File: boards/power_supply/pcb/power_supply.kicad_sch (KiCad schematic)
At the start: 0 parts

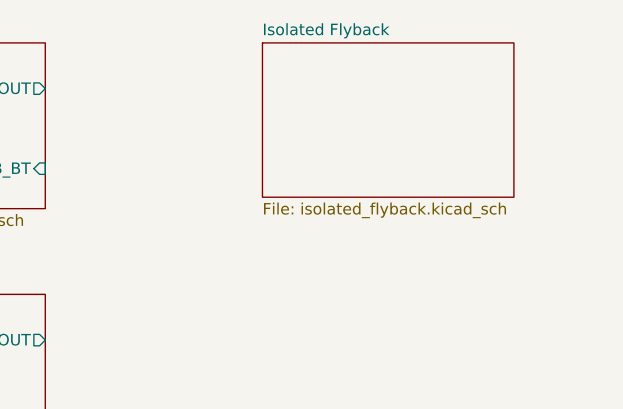
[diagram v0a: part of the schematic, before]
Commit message: psu schematic capture
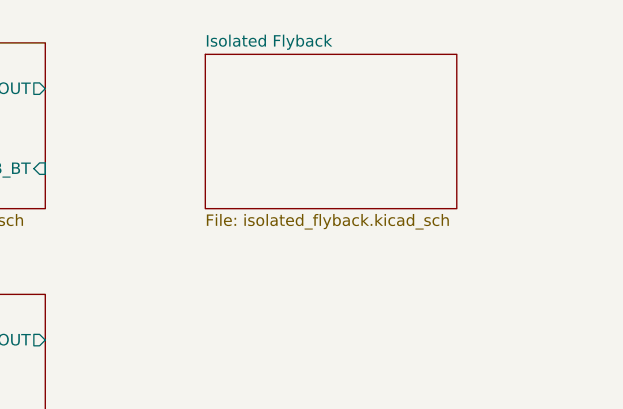
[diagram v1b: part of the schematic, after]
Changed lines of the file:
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@@
 	)
 	(sheet
-		(at 176.53 60.96)
+		(at 170.18 62.23)
 		(size 27.94 17.145)
 		(fields_autoplaced yes)
@@
 		)
 		(property "Sheetname" "Isolated Flyback"
-			(at 176.53 60.2484 0)
+			(at 170.18 61.5184 0)
 			(effects
 				(font
@@
 		)
 		(property "Sheetfile" "isolated_flyback.kicad_sch"
-			(at 176.53 78.6896 0)
+			(at 170.18 79.9596 0)
 			(effects
 				(font

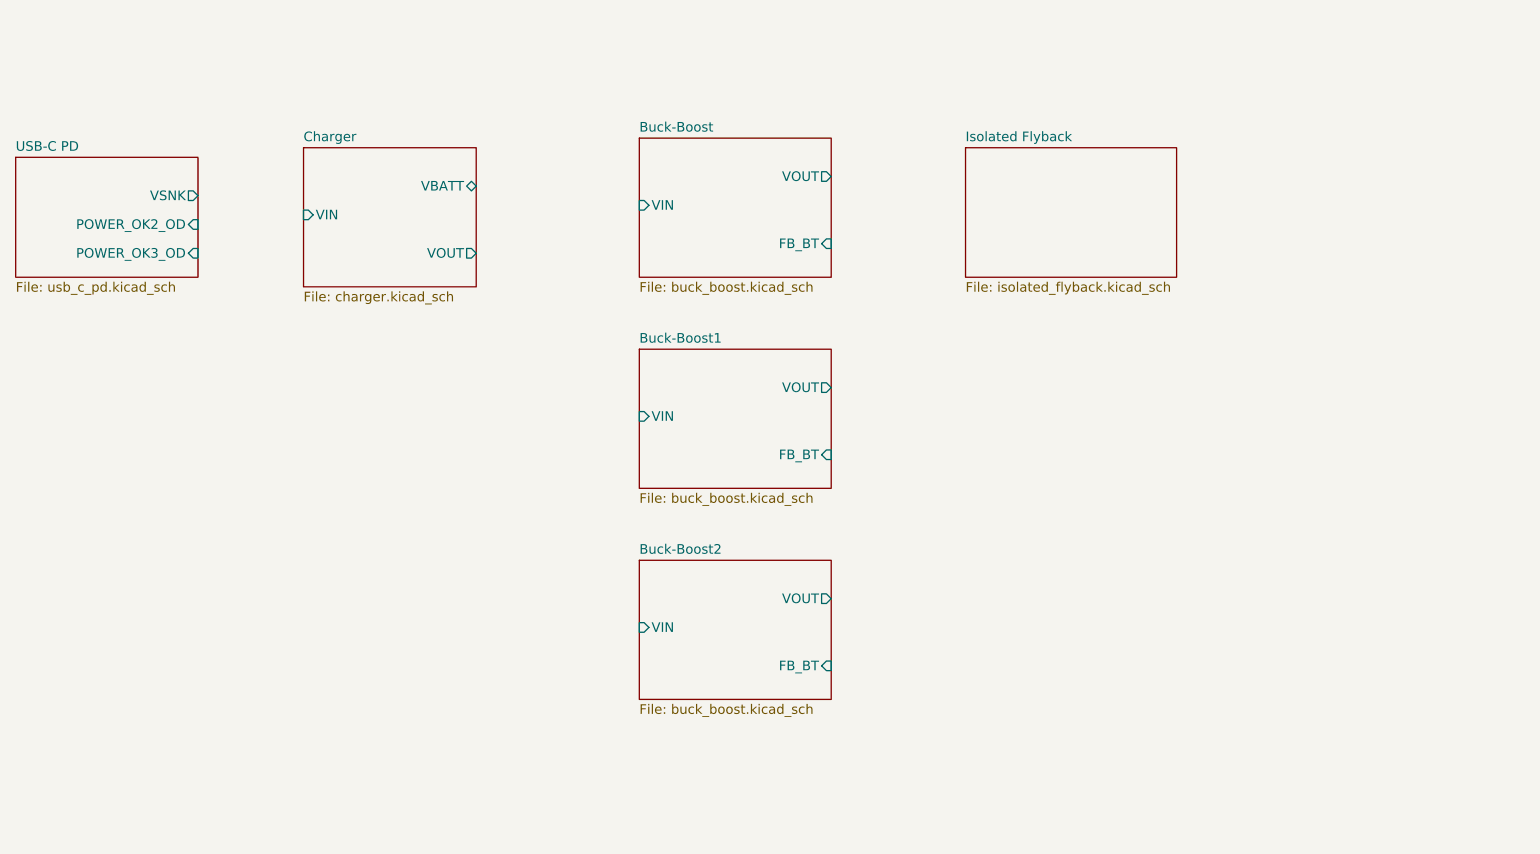
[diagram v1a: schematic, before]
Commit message: psu schematic capture
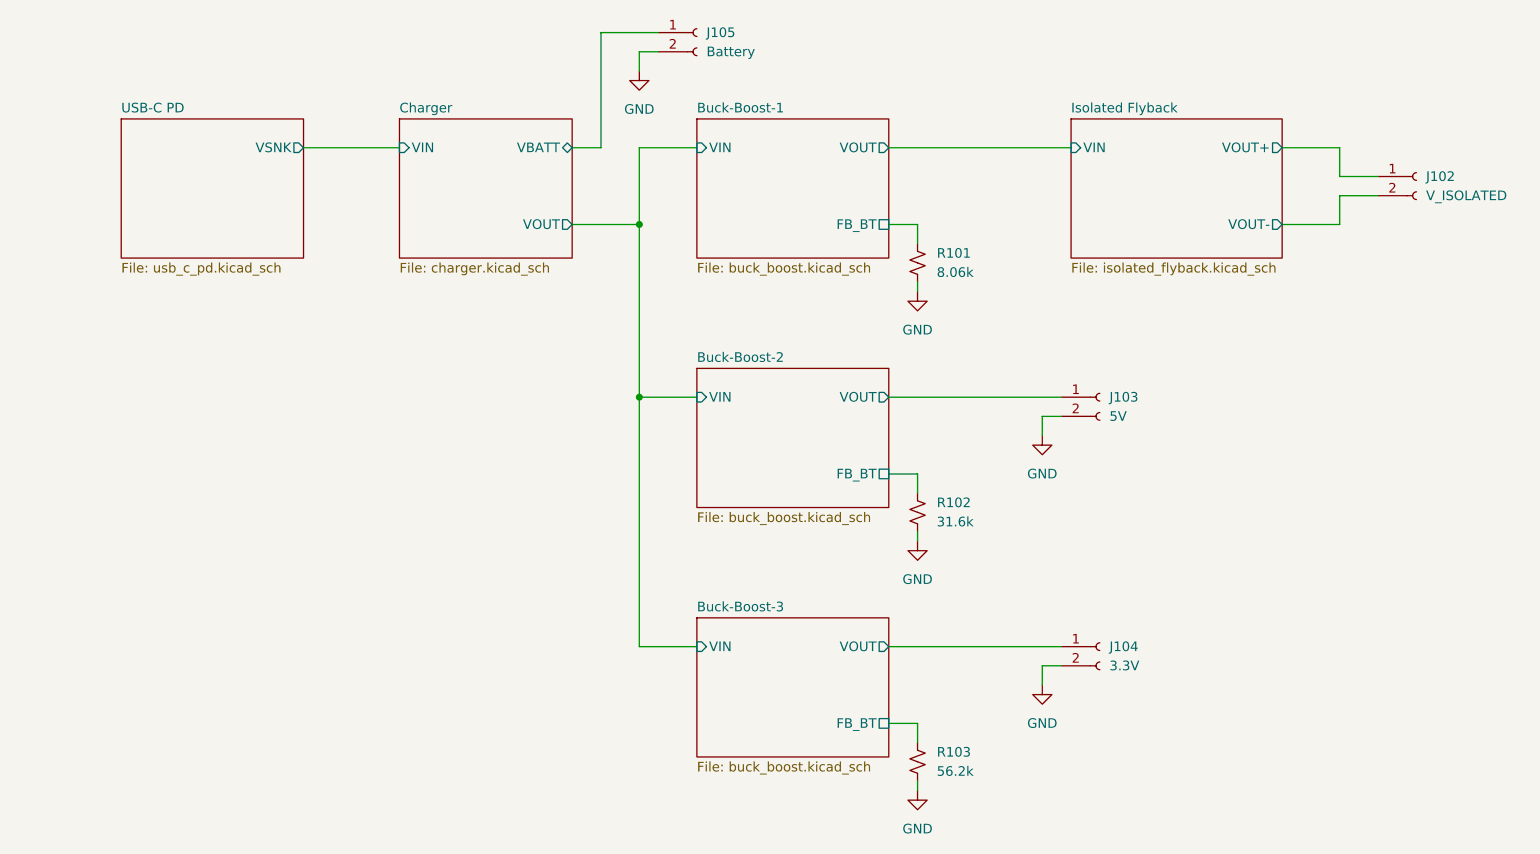
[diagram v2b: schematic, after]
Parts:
- added J102: V_ISOLATED, symbol Connector:Conn_01x02_Socket
- added J103: 5V, symbol Connector:Conn_01x02_Socket
- added J104: 3.3V, symbol Connector:Conn_01x02_Socket
- added J105: Battery, symbol Connector:Conn_01x02_Socket
- added R101: 8.06k, symbol Device:R_Small_US
- added R102: 31.6k, symbol Device:R_Small_US
- added R103: 56.2k, symbol Device:R_Small_US
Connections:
- net Buck-Boost-1/FB_BT: now also R101.2
- net Buck-Boost-2/FB_BT: now also R102.2
- net Buck-Boost-2/VOUT: now also J103.1 (Pin_1)
- net Buck-Boost-3/FB_BT: now also R103.2
- net Buck-Boost-3/VOUT: now also J104.1 (Pin_1)
- net Charger/VBATT: now also J105.1 (Pin_1)
- new net GND: J103.2 (Pin_2), J104.2 (Pin_2), J105.2 (Pin_2), R101.1, R102.1, R103.1
- new net Isolated Flyback/VOUT+: J102.1 (Pin_1)
- new net Isolated Flyback/VOUT-: J102.2 (Pin_2)
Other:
- sheet Buck-Boost renamed Buck-Boost-1
- sheet Buck-Boost1 renamed Buck-Boost-2
- sheet Buck-Boost2 renamed Buck-Boost-3
- sheet Isolated Flyback ports: added VIN, VOUT+, VOUT-; removed none
- sheet USB-C PD ports: added none; removed POWER_OK2_OD, POWER_OK3_OD

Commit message: psu component selection
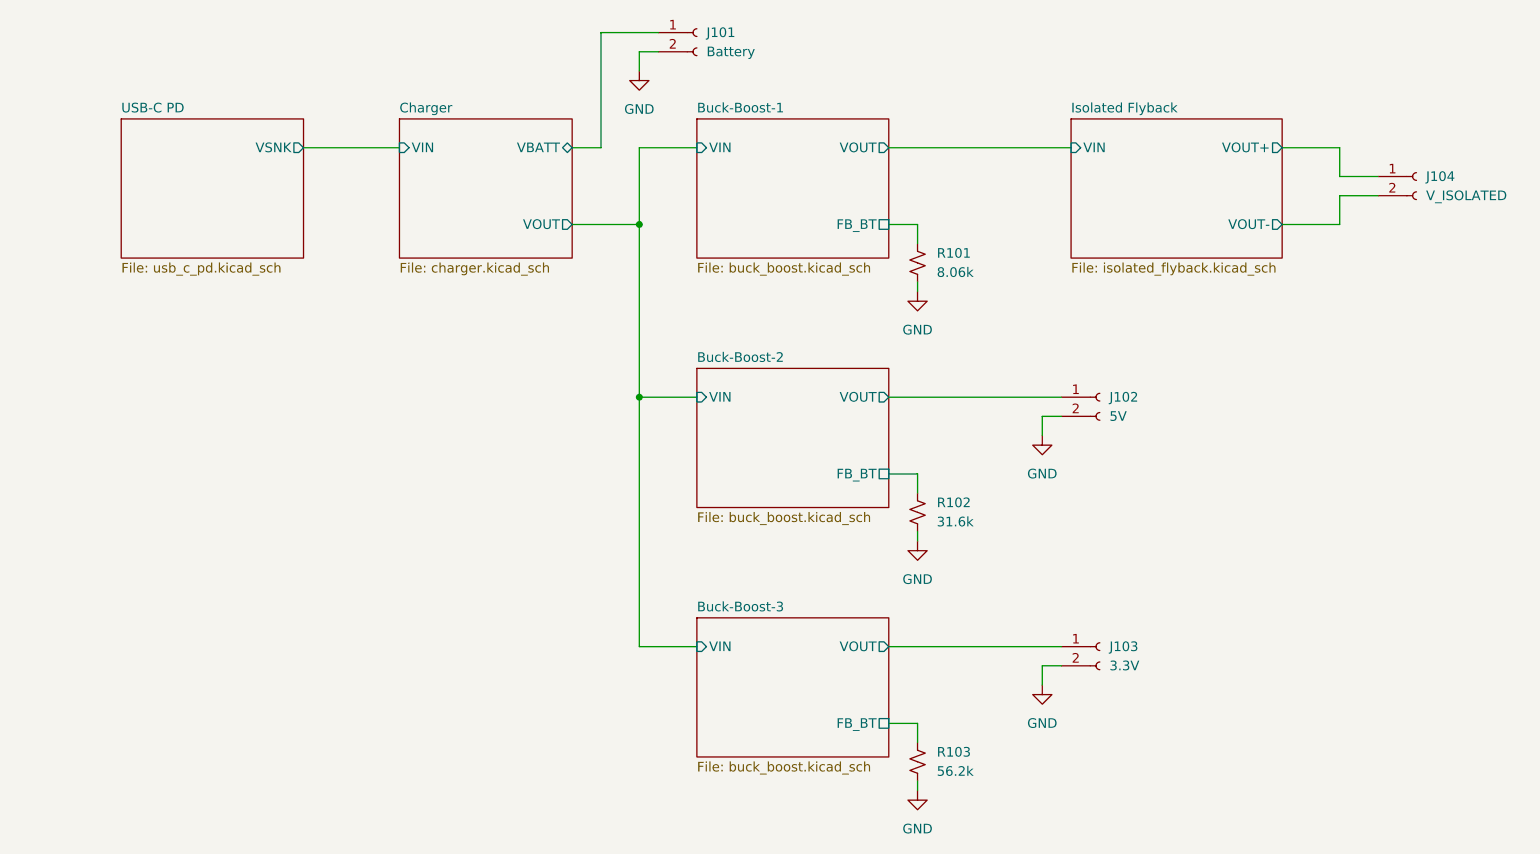
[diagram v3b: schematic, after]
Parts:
- renumbered J105 to J101, J103 to J102, J104 to J103, J102 to J104
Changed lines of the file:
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@@
 		(dnp no)
 		(fields_autoplaced yes)
-		(property "Reference" "J103"
+		(property "Reference" "J102"
 			(at 189.23 95.2499 0)
 			(effects
@@
 			(project "power_supply"
 				(path "/6a7d9dc9-f78f-470f-911b-b95256023173"
-					(reference "J103")
+					(reference "J102")
 					(unit 1)
 				)
@@
 		(dnp no)
 		(fields_autoplaced yes)
-		(property "Reference" "J104"
+		(property "Reference" "J103"
 			(at 189.23 128.2699 0)
 			(effects
@@
 			(project "power_supply"
 				(path "/6a7d9dc9-f78f-470f-911b-b95256023173"
-					(reference "J104")
+					(reference "J103")
 					(unit 1)
 				)
@@
 		(dnp no)
 		(fields_autoplaced yes)
-		(property "Reference" "#PWR0106"
+		(property "Reference" "#PWR0105"
 			(at 180.34 106.68 0)
 			(effects
@@
 			(project "power_supply"
 				(path "/6a7d9dc9-f78f-470f-911b-b95256023173"
-					(reference "#PWR0106")
+					(reference "#PWR0105")
 					(unit 1)
 				)
@@
 		(dnp no)
 		(fields_autoplaced yes)
-		(property "Reference" "J105"
+		(property "Reference" "J101"
 			(at 135.89 46.9899 0)
 			(effects
@@
 			(project "power_supply"
 				(path "/6a7d9dc9-f78f-470f-911b-b95256023173"
-					(reference "J105")
+					(reference "J101")
 					(unit 1)
 				)
@@
 		(dnp no)
 		(fields_autoplaced yes)
-		(property "Reference" "#PWR0105"
+		(property "Reference" "#PWR0106"
 			(at 180.34 139.7 0)
 			(effects
@@
 			(project "power_supply"
 				(path "/6a7d9dc9-f78f-470f-911b-b95256023173"
-					(reference "#PWR0105")
+					(reference "#PWR0106")
 					(unit 1)
 				)
@@
 		(dnp no)
 		(fields_autoplaced yes)
-		(property "Reference" "J102"
+		(property "Reference" "J104"
 			(at 231.14 66.0399 0)
 			(effects
@@
 			(project ""
 				(path "/6a7d9dc9-f78f-470f-911b-b95256023173"
-					(reference "J102")
-					(unit 1)
-				)
+					(reference "J104")
+					(unit 1)
+				)

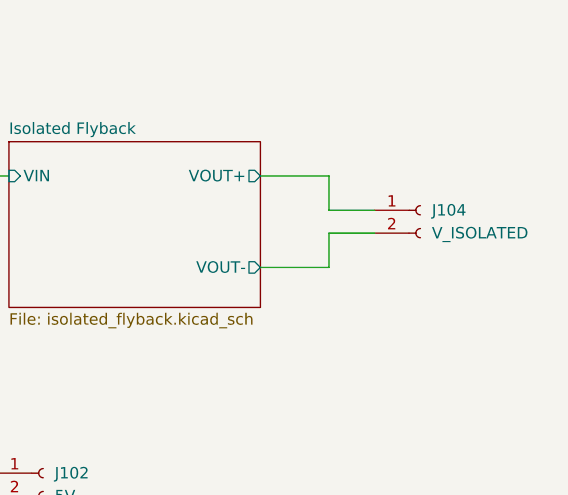
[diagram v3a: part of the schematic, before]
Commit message: created psu footprints
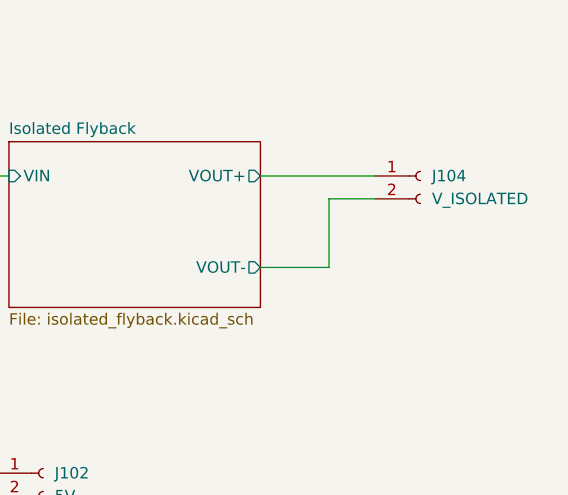
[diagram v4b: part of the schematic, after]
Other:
- moved on the sheet: J104
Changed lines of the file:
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@@
-	(wire
-		(pts
-			(xy 224.79 66.04) (xy 219.71 66.04)
-		)
-		(stroke
-			(width 0)
-			(type default)
-		)
-	)
 	(wire
 		(pts
@@
 	(wire
 		(pts
-			(xy 219.71 68.58) (xy 219.71 72.39)
+			(xy 219.71 64.77) (xy 219.71 72.39)
 		)
 		(stroke
@@
 	(wire
 		(pts
-			(xy 224.79 68.58) (xy 219.71 68.58)
+			(xy 224.79 64.77) (xy 219.71 64.77)
 		)
 		(stroke
@@
 	(wire
 		(pts
-			(xy 219.71 66.04) (xy 219.71 62.23)
-		)
-		(stroke
-			(width 0)
-			(type default)
-		)
-	)
-	(wire
-		(pts
 			(xy 180.34 130.81) (xy 180.34 133.35)
 		)
@@
 	(wire
 		(pts
-			(xy 212.09 62.23) (xy 219.71 62.23)
+			(xy 212.09 62.23) (xy 224.79 62.23)
 		)
 		(stroke
@@
 	(symbol
 		(lib_id "Connector:Conn_01x02_Socket")
-		(at 229.87 66.04 0)
+		(at 229.87 62.23 0)
 		(unit 1)
 		(exclude_from_sim no)
@@
 		(fields_autoplaced yes)
 		(property "Reference" "J104"
-			(at 231.14 66.0399 0)
+			(at 231.14 62.2299 0)
 			(effects
 				(font
@@
 		)
 		(property "Value" "V_ISOLATED"
-			(at 231.14 68.5799 0)
+			(at 231.14 64.7699 0)
 			(effects
 				(font
@@
 		)
 		(property "Footprint" ""
-			(at 229.87 66.04 0)
+			(at 229.87 62.23 0)
 			(effects
 				(font
@@
 		)
 		(property "Datasheet" "~"
-			(at 229.87 66.04 0)
+			(at 229.87 62.23 0)
 			(effects
 				(font
@@
 		)
 		(property "Description" "Generic connector, single row, 01x02, script generated"
-			(at 229.87 66.04 0)
-			(effects
-				(font
+			(at 229.87 62.23 0)
+			(effects
+				(font

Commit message: starting psu layout
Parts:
- J101: footprint (none) -> Connector_AMASS:AMASS_XT30U-F_1x02_P5.0mm_Vertical
- J102, J103, J104: footprint (none) -> Connector_PinHeader_2.54mm:PinHeader_1x02_P2.54mm_Vertical
- R101, R102, R103: footprint (none) -> Resistor_SMD:R_0603_1608Metric
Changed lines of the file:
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@@
 			)
 		)
-		(property "Footprint" ""
+		(property "Footprint" "Resistor_SMD:R_0603_1608Metric"
 			(at 163.83 110.49 0)
 			(effects
@@
 			)
 		)
-		(property "Footprint" ""
+		(property "Footprint" "Connector_PinHeader_2.54mm:PinHeader_1x02_P2.54mm_Vertical"
 			(at 187.96 95.25 0)
 			(effects
@@
 			)
 		)
-		(property "Footprint" ""
+		(property "Footprint" "Connector_PinHeader_2.54mm:PinHeader_1x02_P2.54mm_Vertical"
 			(at 187.96 128.27 0)
 			(effects
@@
 			)
 		)
-		(property "Footprint" ""
+		(property "Footprint" "Connector_AMASS:AMASS_XT30U-F_1x02_P5.0mm_Vertical"
 			(at 134.62 46.99 0)
 			(effects
@@
 			)
 		)
-		(property "Footprint" ""
+		(property "Footprint" "Resistor_SMD:R_0603_1608Metric"
 			(at 163.83 143.51 0)
 			(effects
@@
 			)
 		)
-		(property "Footprint" ""
+		(property "Footprint" "Connector_PinHeader_2.54mm:PinHeader_1x02_P2.54mm_Vertical"
 			(at 229.87 62.23 0)
 			(effects
@@
 			)
 		)
-		(property "Footprint" ""
+		(property "Footprint" "Resistor_SMD:R_0603_1608Metric"
 			(at 163.83 77.47 0)
 			(effects

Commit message: initial psu charger layout
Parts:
- J101: footprint Connector_AMASS:AMASS_XT30U-F_1x02_P5.0mm_Vertical -> xt30:AMASS_XT30U-F_1x02_P5.0mm_Vertical
- J102, J103, J104: footprint Connector_PinHeader_2.54mm:PinHeader_1x02_P2.54mm_Vertical -> Connector_JST:JST_XH_B2B-XH-A_1x02_P2.50mm_Vertical
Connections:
- net Charger/VBATT: now also J101.2 (Pin_2); no longer J101.1 (Pin_1)
- net GND: now also J101.1 (Pin_1); no longer J101.2 (Pin_2)
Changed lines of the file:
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@@
-	(wire
-		(pts
-			(xy 129.54 46.99) (xy 121.92 46.99)
-		)
-		(stroke
-			(width 0)
-			(type default)
-		)
-	)
 	(wire
 		(pts
@@
 		(pts
 			(xy 163.83 107.95) (xy 163.83 105.41)
+		)
+		(stroke
+			(width 0)
+			(type default)
+		)
+	)
+	(wire
+		(pts
+			(xy 121.92 46.99) (xy 129.54 46.99)
 		)
 		(stroke
@@
 			)
 		)
-		(property "Footprint" "Connector_PinHeader_2.54mm:PinHeader_1x02_P2.54mm_Vertical"
+		(property "Footprint" "Connector_JST:JST_XH_B2B-XH-A_1x02_P2.50mm_Vertical"
 			(at 187.96 95.25 0)
 			(effects
@@
 			)
 		)
-		(property "Footprint" "Connector_PinHeader_2.54mm:PinHeader_1x02_P2.54mm_Vertical"
+		(property "Footprint" "Connector_JST:JST_XH_B2B-XH-A_1x02_P2.50mm_Vertical"
 			(at 187.96 128.27 0)
 			(effects
@@
 	(symbol
 		(lib_id "Connector:Conn_01x02_Socket")
-		(at 134.62 46.99 0)
-		(unit 1)
-		(exclude_from_sim no)
-		(in_bom yes)
-		(on_board yes)
-		(dnp no)
-		(fields_autoplaced yes)
+		(at 134.62 49.53 0)
+		(mirror x)
+		(unit 1)
+		(exclude_from_sim no)
+		(in_bom yes)
+		(on_board yes)
+		(dnp no)
 		(property "Reference" "J101"
-			(at 135.89 46.9899 0)
+			(at 135.89 49.5301 0)
 			(effects
 				(font
@@
 		)
 		(property "Value" "Battery"
-			(at 135.89 49.5299 0)
+			(at 135.89 46.9901 0)
 			(effects
 				(font
@@
 			)
 		)
-		(property "Footprint" "Connector_AMASS:AMASS_XT30U-F_1x02_P5.0mm_Vertical"
-			(at 134.62 46.99 0)
+		(property "Footprint" "xt30:AMASS_XT30U-F_1x02_P5.0mm_Vertical"
+			(at 134.62 49.53 0)
 			(effects
 				(font
@@
 		)
 		(property "Datasheet" "~"
-			(at 134.62 46.99 0)
+			(at 134.62 49.53 0)
 			(effects
 				(font
@@
 		)
 		(property "Description" "Generic connector, single row, 01x02, script generated"
-			(at 134.62 46.99 0)
+			(at 134.62 49.53 0)
 			(effects
 				(font
@@
 			)
 		)
-		(property "Footprint" "Connector_PinHeader_2.54mm:PinHeader_1x02_P2.54mm_Vertical"
+		(property "Footprint" "Connector_JST:JST_XH_B2B-XH-A_1x02_P2.50mm_Vertical"
 			(at 229.87 62.23 0)
 			(effects
